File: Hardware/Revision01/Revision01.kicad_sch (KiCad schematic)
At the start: 32 parts, among them J1 Battery connector, SW2 SW_SPST_LED, U10 NCP1117LPST50T3G, U3 NUCLEO-L476RG

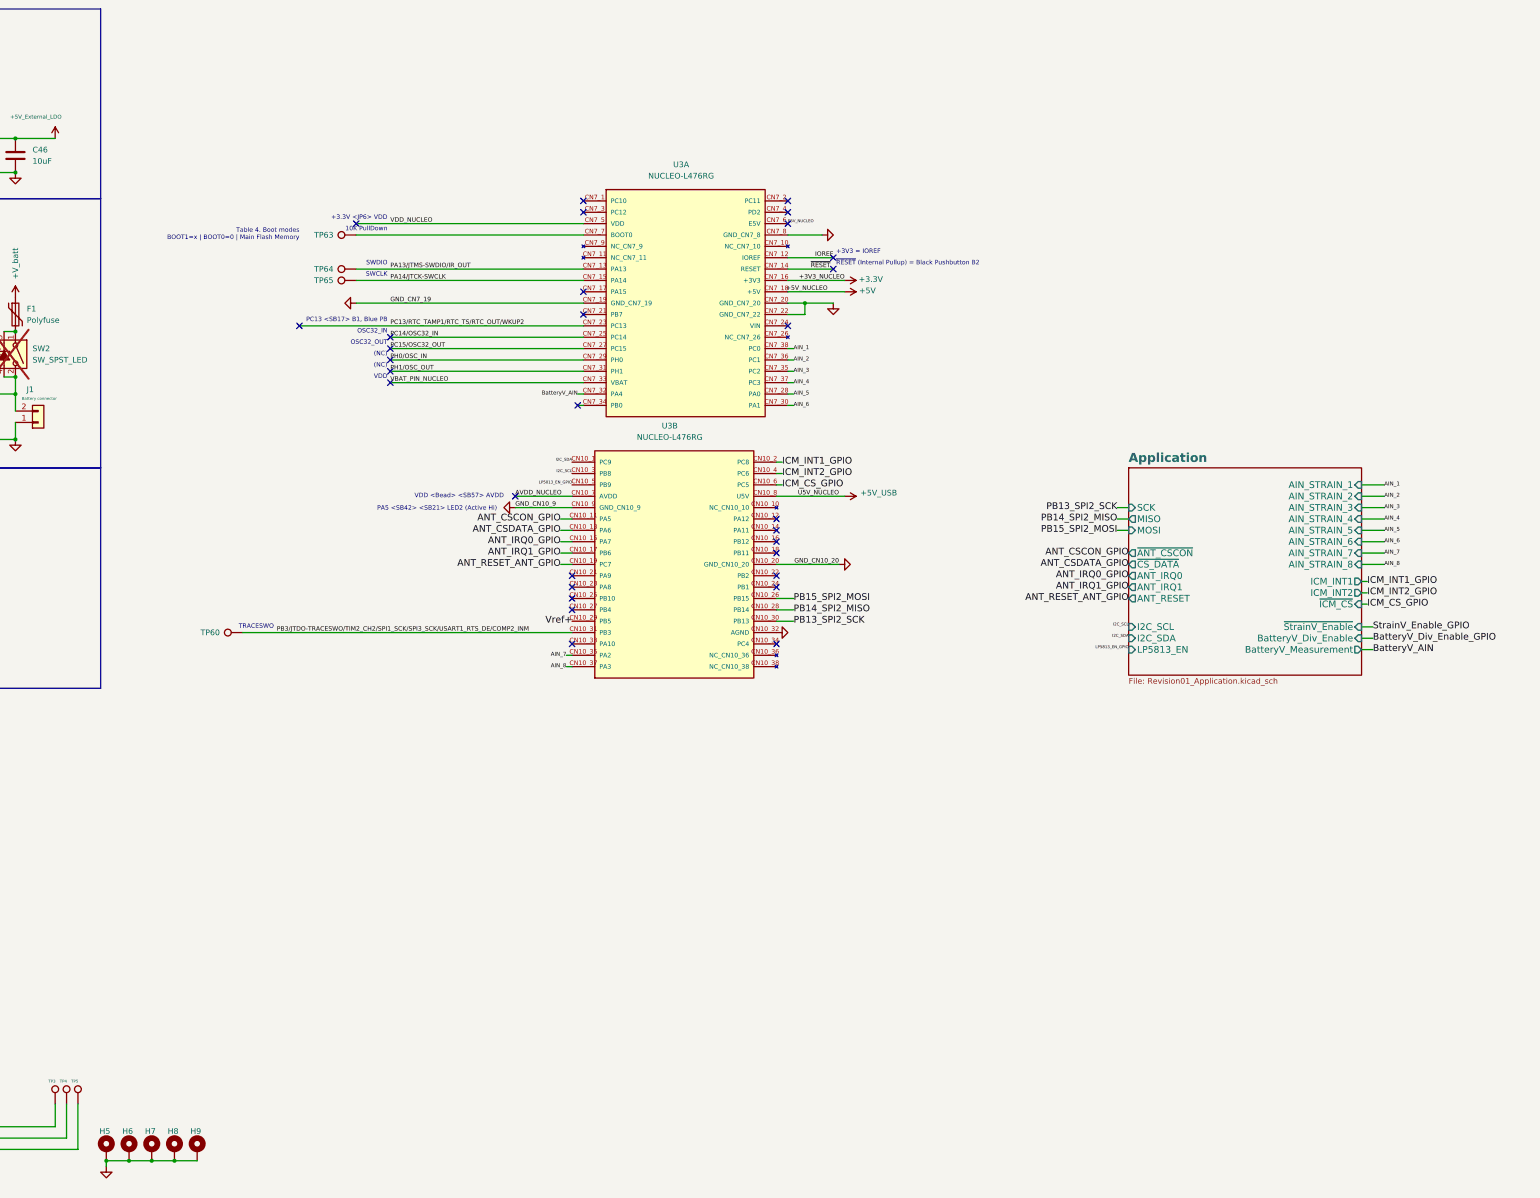
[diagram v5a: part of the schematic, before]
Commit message: schematic wiring, and LT-SPICE simulations on strain gauge - Added buffer with offset at 1.66V to instrumentation amplifier to ensure -20-20mv range can be read - Added caps to Instrumentation Amplifier circuit - Stimulated straingauge->Amplifier->Adc with all components imported. Verified ADC can read between 0.3-3.0V - Created second draft bom, component cost at around 212$ - Changed many components to Automotive grade - Added breathingCUBE led driver to prototype my own project
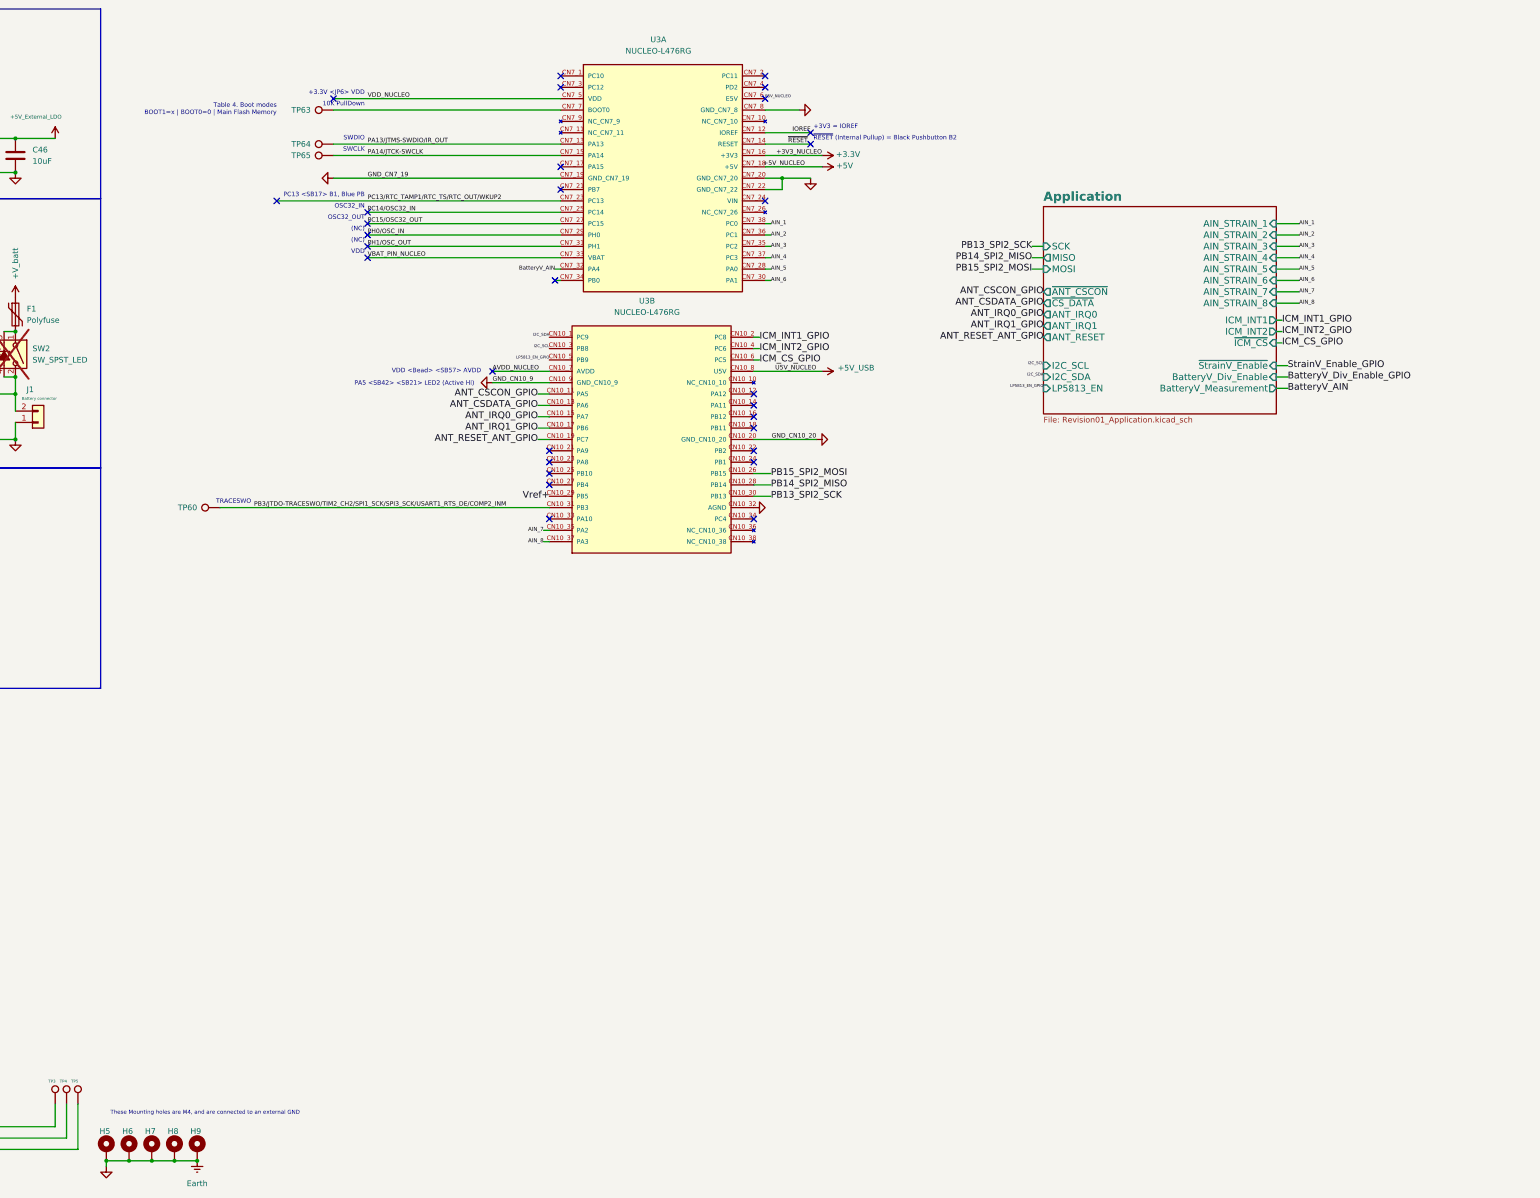
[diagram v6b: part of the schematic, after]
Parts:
- BT1, BT2, BT3, BT4: Quantity 4 -> (none)
- C46, C47: Price per unit 0.15 -> 4; Quantity 3 -> (none)
- D3, D5, F1, J1, N1: Quantity 1 -> (none)
- H5, H6, H7, H8, H9: footprint (none) -> MountingHole:MountingHole_4.3mm_M4_ISO7380_Pad_TopBottom
- R11, R13: Distributor link https://www.digikey.ca/en/products/detail/bourns-inc/CR0805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 -> https://www.mouser.ca/ProductDetail/Bourns/CR0805-JW-331ELF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; Quantity 2 -> (none)
- SW2: Distributor link https://www.digikey.ca/en/products/detail/e-switch/RR111311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 -> https://www.mouser.ca/ProductDetail/E-Switch/RR11131100-214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; Price per unit 2.1 -> 2.04; Quantity 1 -> (none)
- U10: Price per unit 1.29 -> 1.25; Quantity 1 -> (none)
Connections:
- net GND renamed Earth
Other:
- note added: "These Mounting holes are M4, and are connected to an external GND"
- moved on the sheet: TP60, TP63, TP64, TP65, U3A, U3B

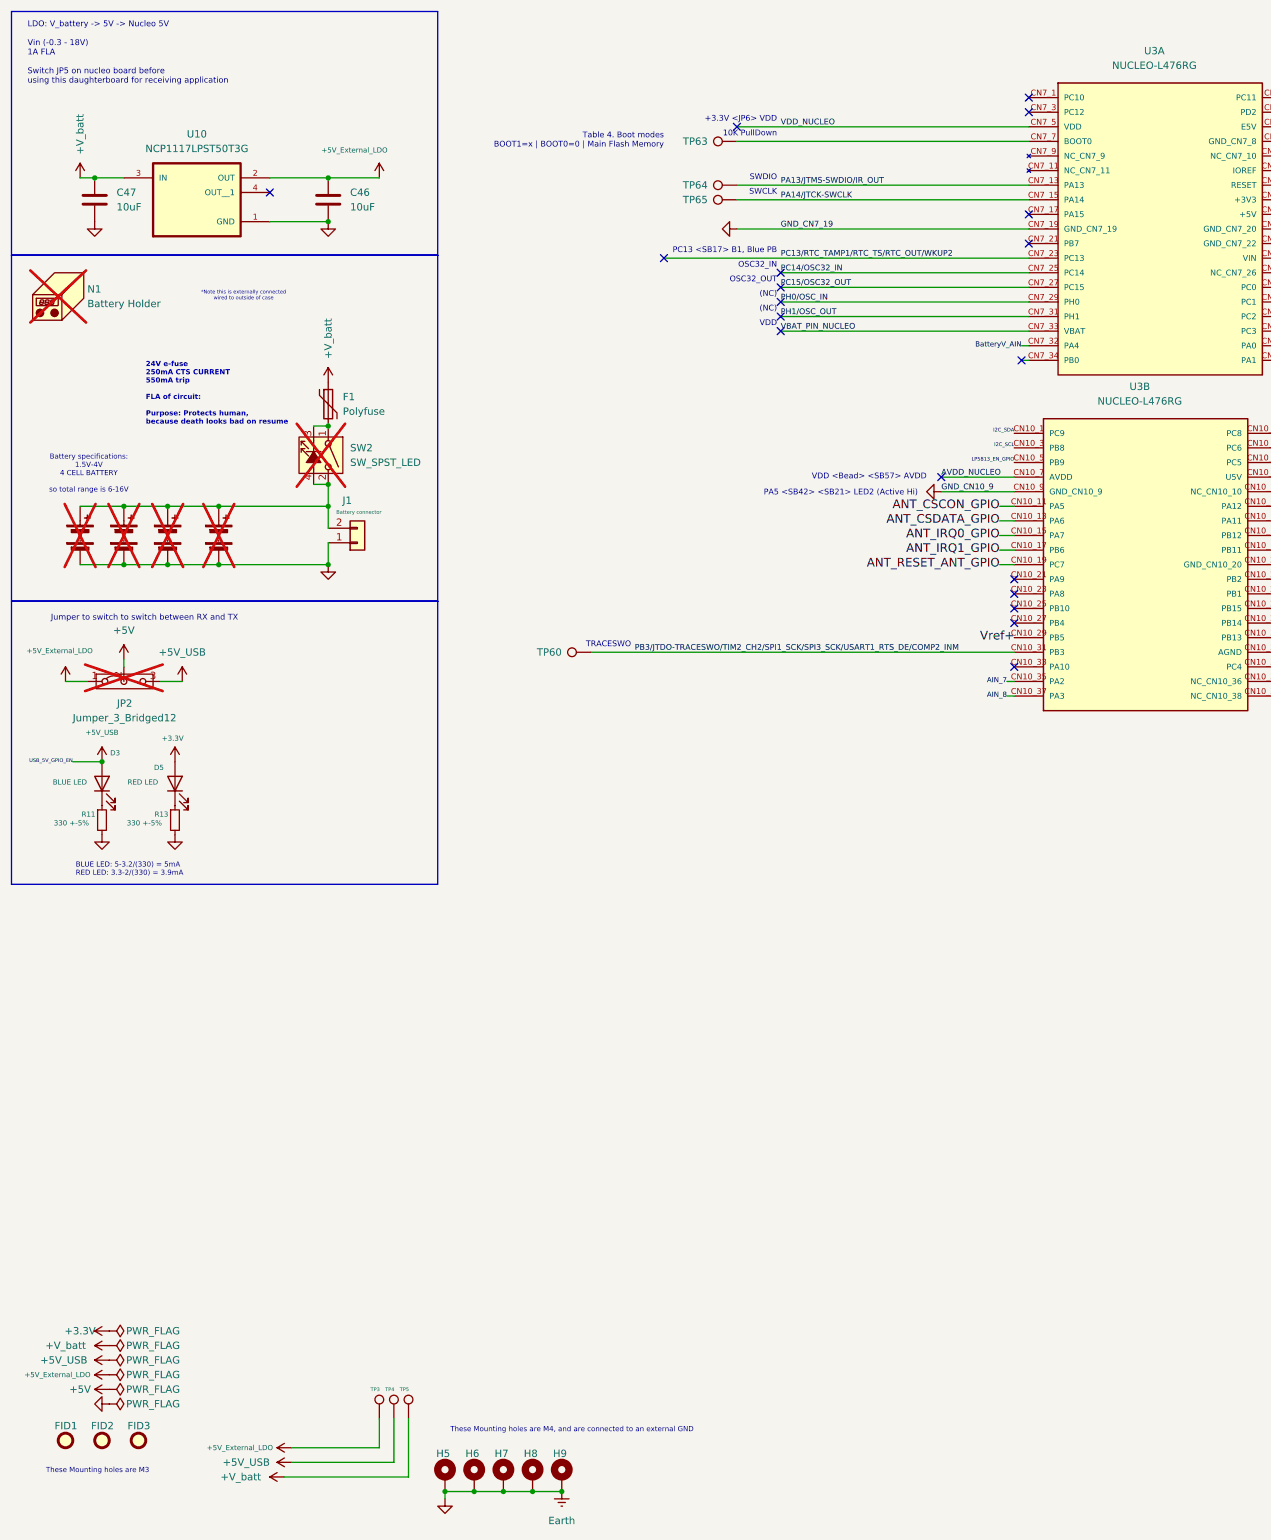
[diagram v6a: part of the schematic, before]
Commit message: branch fuses selected. Ready for PCB layout
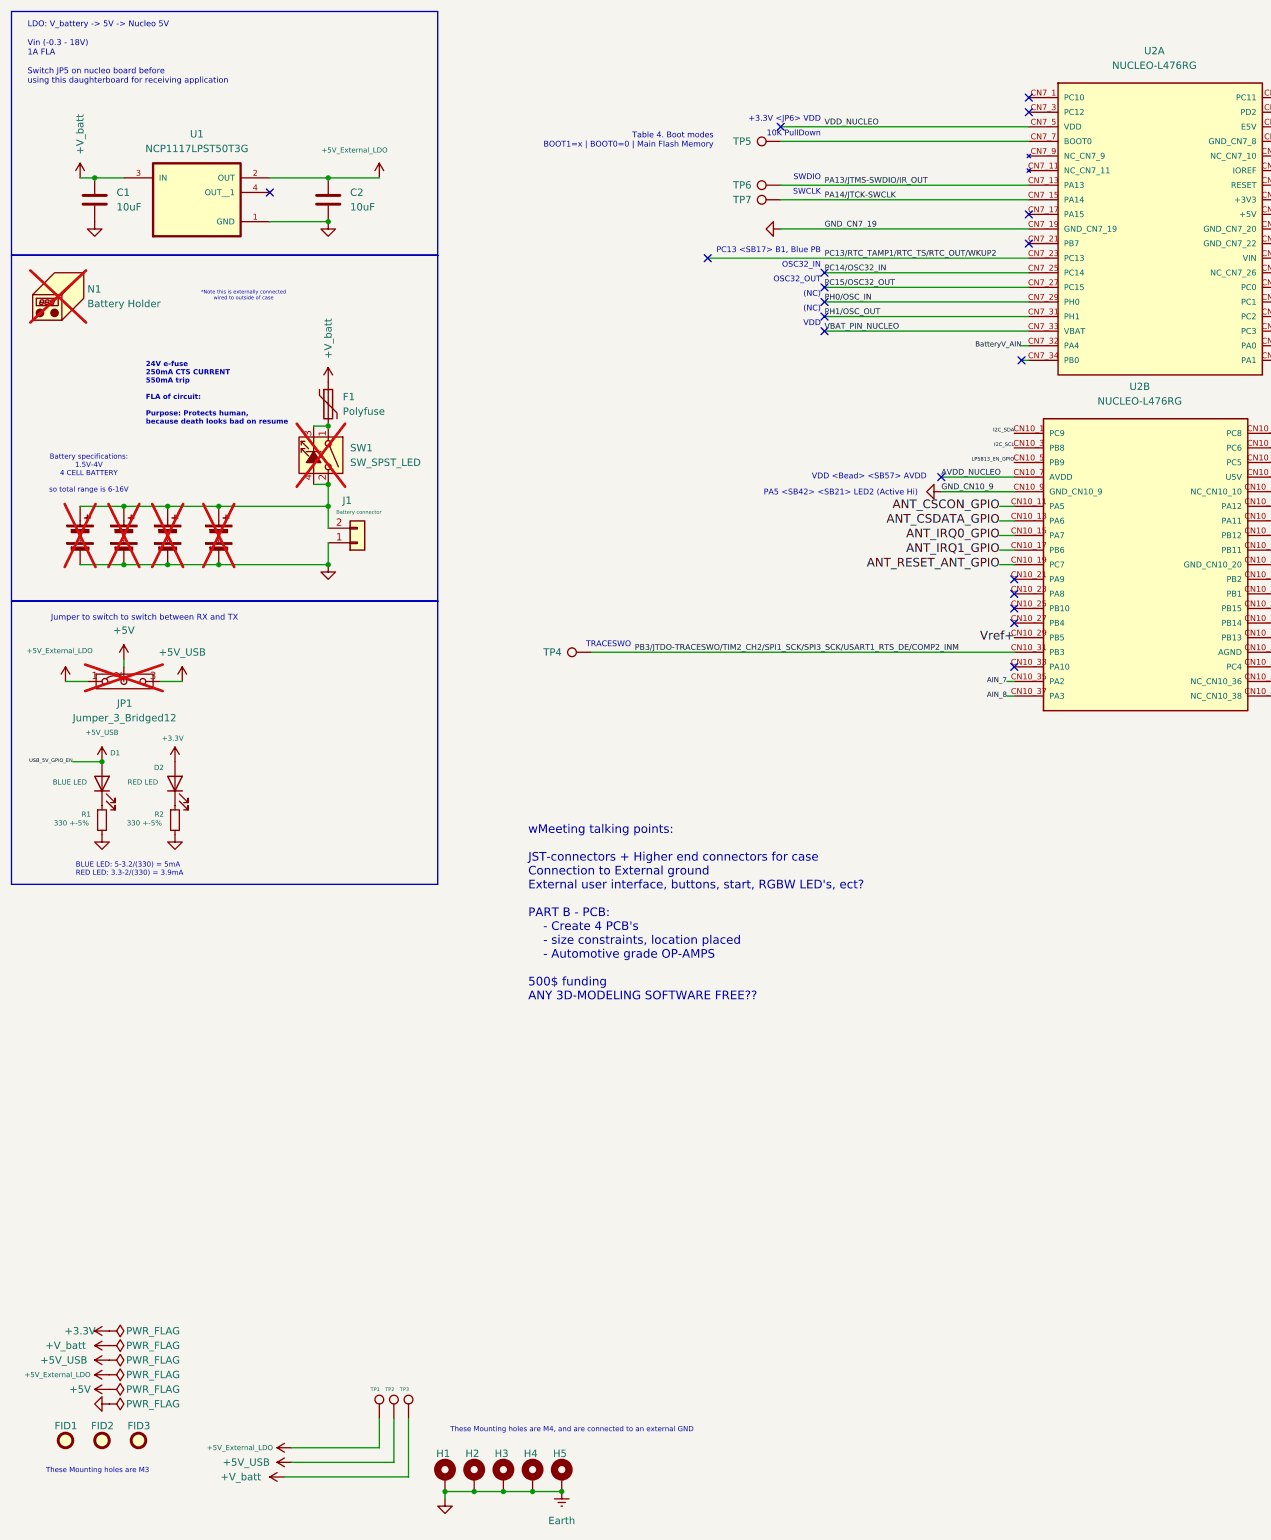
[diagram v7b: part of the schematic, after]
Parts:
- C1: renamed from C47; footprint Capacitor_SMD:C_1206_3216Metric -> Capacitor_SMD:C_1206_3216Metric_Pad1.33x1.80mm_HandSolder; Distributor link https://www.digikey.ca/en/products/detail/murata-electronic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 -> https://www.digikey.ca/en/products/detail/samsung-electro-m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; Price per unit 4 -> 0.15
- C2: renamed from C46; footprint Capacitor_SMD:C_1206_3216Metric -> Capacitor_SMD:C_1206_3216Metric_Pad1.33x1.80mm_HandSolder; Distributor link https://www.digikey.ca/en/products/detail/murata-electronic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 -> https://www.digikey.ca/en/products/detail/samsung-electro-m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; Price per unit 4 -> 0.15
- renumbered BT4 to BT1, BT3 to BT2, BT2 to BT3, BT1 to BT4, D3 to D1, D5 to D2, H5 to H1, H6 to H2, H7 to H3, H8 to H4, H9 to H5, JP2 to JP1, R11 to R1, R13 to R2, SW2 to SW1, TP3 to TP1, TP4 to TP2, TP5 to TP3, TP60 to TP4, TP63 to TP5, TP64 to TP6, TP65 to TP7, U10 to U1, U3 to U2
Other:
- note added: "wMeeting talking points: JST-connectors + Higher end connectors for case Connection to External ground External user interface, buttons, start, RGBW LED's, ect? PART B - PCB: - Create 4 PCB's - size constraints, location placed - Automotive grade OP-AMPS 500$ funding ANY 3D-MODELING SOFTWARE FREE??"
- moved on the sheet: TP5, TP6, TP7
